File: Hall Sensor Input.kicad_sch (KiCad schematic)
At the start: 3 parts

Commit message: Getting ready for fab
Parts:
- C?: DigiKey (none) -> 490-4762-1-ND
- R? (x2): DigiKey (none) -> 311-1.00KLRCT-ND
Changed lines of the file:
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@@
     (rev "0")
     (company "Cornell High Energy Synchrotron Source")
+    (comment 1 "Hall Sensor Input Filtering")
     (comment 3 "S. Bywater")
     (comment 4 "S. Bywater")
@@
     )
     (property "Comments" "" (at 146.05 107.95 0)
+      (effects (font (size 1.27 1.27)) hide)
+    )
+    (property "DigiKey" "490-4762-1-ND" (at 146.05 107.95 0)
+      (effects (font (size 1.27 1.27)) hide)
+    )
+    (property "LCSC" "" (at 146.05 107.95 0)
       (effects (font (size 1.27 1.27)) hide)
     )
@@
       (effects (font (size 1.27 1.27)) hide)
     )
+    (property "DigiKey" "311-1.00KLRCT-ND" (at 139.7 107.95 0)
+      (effects (font (size 1.27 1.27)) hide)
+    )
+    (property "LCSC" "" (at 139.7 107.95 0)
+      (effects (font (size 1.27 1.27)) hide)
+    )
     (pin "1")
     (pin "2")
@@
       (effects (font (size 1.27 1.27)) hide)
     )
+    (property "DigiKey" "311-1.00KLRCT-ND" (at 133.35 101.6 0)
+      (effects (font (size 1.27 1.27)) hide)
+    )
+    (property "LCSC" "" (at 133.35 101.6 0)
+      (effects (font (size 1.27 1.27)) hide)
+    )

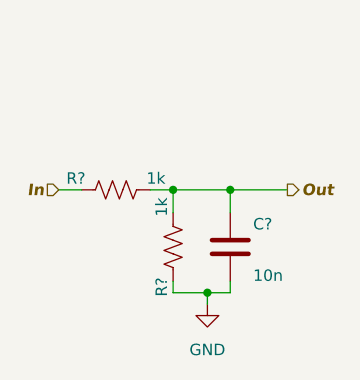
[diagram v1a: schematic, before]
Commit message: Update hall sensor circuit for 5V-tolerant pins
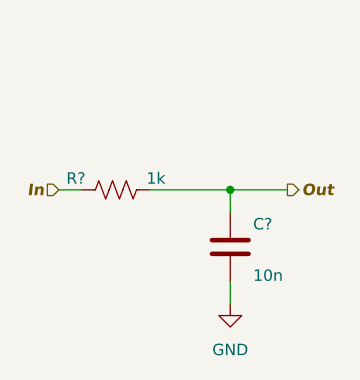
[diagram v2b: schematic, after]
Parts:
- removed R?: 1k, Resistor_SMD:R_0402_1005Metric, symbol Device:R_US
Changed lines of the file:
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@@
   (junction (at 146.05 101.6) (diameter 0) (color 0 0 0 0)
   )
-  (junction (at 139.7 101.6) (diameter 0) (color 0 0 0 0)
-  )
-  (junction (at 143.51 113.03) (diameter 0) (color 0 0 0 0)
-  )
-  (wire (pts (xy 146.05 111.76) (xy 146.05 113.03))
-    (stroke (width 0) (type default))
-  )
-  (wire (pts (xy 139.7 101.6) (xy 139.7 104.14))
+  (wire (pts (xy 146.05 111.76) (xy 146.05 114.3))
     (stroke (width 0) (type default))
   )
@@
     (stroke (width 0) (type default))
   )
-  (wire (pts (xy 143.51 113.03) (xy 146.05 113.03))
-    (stroke (width 0) (type default))
-  )
-  (wire (pts (xy 139.7 101.6) (xy 146.05 101.6))
+  (wire (pts (xy 137.16 101.6) (xy 146.05 101.6))
     (stroke (width 0) (type default))
   )
   (wire (pts (xy 146.05 101.6) (xy 152.4 101.6))
-    (stroke (width 0) (type default))
-  )
-  (wire (pts (xy 139.7 111.76) (xy 139.7 113.03))
-    (stroke (width 0) (type default))
-  )
-  (wire (pts (xy 139.7 113.03) (xy 143.51 113.03))
-    (stroke (width 0) (type default))
-  )
-  (wire (pts (xy 137.16 101.6) (xy 139.7 101.6))
-    (stroke (width 0) (type default))
-  )
-  (wire (pts (xy 143.51 113.03) (xy 143.51 114.3))
     (stroke (width 0) (type default))
   )
@@
     )
   )
-  (symbol (lib_id "power:GND") (at 143.51 114.3 0) (unit 1)
+  (symbol (lib_id "power:GND") (at 146.05 114.3 0) (unit 1)
     (in_bom yes) (on_board yes) (dnp no) (fields_autoplaced)
-    (property "Reference" "#PWR068" (at 143.51 120.65 0)
+    (property "Reference" "#PWR068" (at 146.05 120.65 0)
       (effects (font (size 1.27 1.27)) hide)
     )
-    (property "Value" "GND" (at 143.51 119.38 0)
+    (property "Value" "GND" (at 146.05 119.38 0)
       (effects (font (size 1.27 1.27)))
     )
-    (property "Footprint" "" (at 143.51 114.3 0)
+    (property "Footprint" "" (at 146.05 114.3 0)
       (effects (font (size 1.27 1.27)) hide)
     )
-    (property "Datasheet" "" (at 143.51 114.3 0)
+    (property "Datasheet" "" (at 146.05 114.3 0)
       (effects (font (size 1.27 1.27)) hide)
     )
@@
         )
       )
-    )
-  )
-  (symbol (lib_id "Device:R_US") (at 139.7 107.95 180) (unit 1)
-    (in_bom yes) (on_board yes) (dnp no)
-    (property "Reference" "R?" (at 138.43 112.395 90)
-      (effects (font (size 1.27 1.27)))
-    )
-    (property "Value" "1k" (at 138.43 103.505 90)
-      (effects (font (size 1.27 1.27)))
-    )
-    (property "Footprint" "Resistor_SMD:R_0402_1005Metric" (at 138.684 107.696 90)
-      (effects (font (size 1.27 1.27)) hide)
-    )
-    (property "Datasheet" "~" (at 139.7 107.95 0)
-      (effects (font (size 1.27 1.27)) hide)
-    )
-    (property "Comments" "" (at 139.7 107.95 0)
-      (effects (font (size 1.27 1.27)) hide)
-    )
-    (property "DigiKey" "311-1.00KLRCT-ND" (at 139.7 107.95 0)
-      (effects (font (size 1.27 1.27)) hide)
-    )
-    (property "LCSC" "" (at 139.7 107.95 0)
-      (effects (font (size 1.27 1.27)) hide)
-    )
-    (pin "1")
-    (pin "2")
-    (instances
-      (project "ECE4760 Motor Driver"
-        (path "/6b38a626-de8c-4b2d-bc76-3a02bc823a86"
-          (reference "R?") (unit 1)
-        )
-        (path "/6b38a626-de8c-4b2d-bc76-3a02bc823a86/9e0a8a8b-b0ec-4703-8f8c-5ea275317857"
-          (reference "R13") (unit 1)
-        )
-        (path "/6b38a626-de8c-4b2d-bc76-3a02bc823a86/cdc8f404-9c8e-42d0-adf1-2d432268a04d"
-          (reference "R15") (unit 1)
-        )
-        (path "/6b38a626-de8c-4b2d-bc76-3a02bc823a86/a05ea58c-77e1-4772-b7c7-450b1547e96e"
-          (reference "R17") (unit 1)
-        )
-        (path "/6b38a626-de8c-4b2d-bc76-3a02bc823a86/719c509b-8ff9-4083-837d-a3024db7e531"
-          (reference "R19") (unit 1)
-        )
-      )

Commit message: Ready for design review
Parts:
- added D?: BAT54XY, Package_TO_SOT_SMD:SOT-363_SC-70-6, symbol Diode:BAT54SW
- added R?: 4k7, Resistor_SMD:R_0402_1005Metric, symbol Device:R_US
- C?: value 10n -> 1n; DigiKey 490-4762-1-ND -> 490-GCM155R71H102KA37JCT-ND; LCSC (none) -> C1852263
- R?: value 1k -> 100; DigiKey 311-1.00KLRCT-ND -> 311-100JRCT-ND; LCSC (none) -> C106233
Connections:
- net GND: now also D?.1 (A)
- net Out: now also D?.6 (COM), R?.2
- new net +5V: D?.2 (K), R?.1

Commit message: Update
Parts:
- removed D?: BAT54XY, Package_TO_SOT_SMD:SOT-363_SC-70-6, symbol Diode:BAT54SW
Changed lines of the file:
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@@
   (junction (at 146.05 101.6) (diameter 0) (color 0 0 0 0)
   )
-  (junction (at 139.7 101.6) (diameter 0) (color 0 0 0 0)
-  )
-  (junction (at 142.875 114.935) (diameter 0) (color 0 0 0 0)
-  )
-  (junction (at 142.875 88.9) (diameter 0) (color 0 0 0 0)
-  )
-  (wire (pts (xy 139.7 93.98) (xy 139.7 88.9))
-    (stroke (width 0) (type default))
-  )
-  (wire (pts (xy 142.875 114.935) (xy 142.875 115.57))
-    (stroke (width 0) (type default))
-  )
-  (wire (pts (xy 142.875 114.935) (xy 146.05 114.935))
-    (stroke (width 0) (type default))
-  )
-  (wire (pts (xy 146.05 114.935) (xy 146.05 111.76))
-    (stroke (width 0) (type default))
-  )
-  (wire (pts (xy 139.7 114.935) (xy 142.875 114.935))
+  (wire (pts (xy 146.05 114.3) (xy 146.05 111.76))
     (stroke (width 0) (type default))
   )
@@
     (stroke (width 0) (type default))
   )
-  (wire (pts (xy 139.7 109.22) (xy 139.7 114.935))
-    (stroke (width 0) (type default))
-  )
   (wire (pts (xy 146.05 99.06) (xy 146.05 101.6))
     (stroke (width 0) (type default))
   )
-  (wire (pts (xy 142.875 88.9) (xy 146.05 88.9))
-    (stroke (width 0) (type default))
-  )
   (wire (pts (xy 127 101.6) (xy 129.54 101.6))
     (stroke (width 0) (type default))
   )
-  (wire (pts (xy 137.16 101.6) (xy 139.7 101.6))
-    (stroke (width 0) (type default))
-  )
-  (wire (pts (xy 142.875 87.63) (xy 142.875 88.9))
+  (wire (pts (xy 137.16 101.6) (xy 146.05 101.6))
     (stroke (width 0) (type default))
   )
@@
     (stroke (width 0) (type default))
   )
-  (wire (pts (xy 139.7 88.9) (xy 142.875 88.9))
-    (stroke (width 0) (type default))
-  )
   (wire (pts (xy 146.05 88.9) (xy 146.05 91.44))
-    (stroke (width 0) (type default))
-  )
-  (wire (pts (xy 139.7 101.6) (xy 146.05 101.6))
     (stroke (width 0) (type default))
   )
@@
           (reference "C63") (unit 1)
         )
-        (path "/6b38a626-de8c-4b2d-bc76-3a02bc823a86/719c509b-8ff9-4083-837d-a3024db7e531"
-          (reference "C64") (unit 1)
-        )
-      )
-    )
-  )
-  (symbol (lib_id "power:GND") (at 142.875 115.57 0) (unit 1)
+      )
+    )
+  )
+  (symbol (lib_id "power:GND") (at 146.05 114.3 0) (unit 1)
     (in_bom yes) (on_board yes) (dnp no) (fields_autoplaced)
-    (property "Reference" "#PWR02" (at 142.875 121.92 0)
-      (effects (font (size 1.27 1.27)) hide)
-    )
-    (property "Value" "GND" (at 142.875 120.65 0)
-      (effects (font (size 1.27 1.27)) hide)
-    )
-    (property "Footprint" "" (at 142.875 115.57 0)
-      (effects (font (size 1.27 1.27)) hide)
-    )
-    (property "Datasheet" "" (at 142.875 115.57 0)
+    (property "Reference" "#PWR02" (at 146.05 120.65 0)
+      (effects (font (size 1.27 1.27)) hide)
+    )
+    (property "Value" "GND" (at 146.05 119.38 0)
+      (effects (font (size 1.27 1.27)) hide)
+    )
+    (property "Footprint" "" (at 146.05 114.3 0)
+      (effects (font (size 1.27 1.27)) hide)
+    )
+    (property "Datasheet" "" (at 146.05 114.3 0)
       (effects (font (size 1.27 1.27)) hide)
     )
@@
         (path "/6b38a626-de8c-4b2d-bc76-3a02bc823a86/a05ea58c-77e1-4772-b7c7-450b1547e96e"
           (reference "#PWR06") (unit 1)
-        )
-        (path "/6b38a626-de8c-4b2d-bc76-3a02bc823a86/719c509b-8ff9-4083-837d-a3024db7e531"
-          (reference "#PWR08") (unit 1)
         )
       )
@@
           (reference "R?") (unit 1)
         )
-        (path "/6b38a626-de8c-4b2d-bc76-3a02bc823a86/3c576bdf-2a9b-47b5-bf2f-8d65e4282c90"
-          (reference "R?") (unit 1)
-        )
         (path "/6b38a626-de8c-4b2d-bc76-3a02bc823a86/9e0a8a8b-b0ec-4703-8f8c-5ea275317857"
           (reference "R12") (unit 1)
@@
           (reference "R16") (unit 1)
         )
-        (path "/6b38a626-de8c-4b2d-bc76-3a02bc823a86/719c509b-8ff9-4083-837d-a3024db7e531"
-          (reference "R18") (unit 1)
-        )
-      )
-    )
-  )
-  (symbol (lib_id "Diode:BAT54SW") (at 139.7 101.6 90) (unit 1)
-    (in_bom yes) (on_board yes) (dnp no)
-    (property "Reference" "D?" (at 137.795 93.98 90)
-      (effects (font (size 1.27 1.27)) (justify left))
-    )
-    (property "Value" "BAT54XY" (at 137.795 95.885 90)
-      (effects (font (size 1.27 1.27)) (justify left))
-    )
-    (property "Footprint" "Package_TO_SOT_SMD:SOT-363_SC-70-6" (at 143.51 101.6 0)
-      (effects (font (size 1.27 1.27)) (justify left) hide)
-    )
-    (property "Datasheet" "https://assets.nexperia.com/documents/data-sheet/BAT54W_SER.pdf" (at 143.51 101.6 0)
-      (effects (font (size 1.27 1.27)) hide)
-    )
-    (property "LCSC" "C282367" (at 139.7 101.6 0)
-      (effects (font (size 1.27 1.27)) hide)
-    )
-    (property "DigiKey" "1727-3571-1-ND" (at 139.7 101.6 0)
-      (effects (font (size 1.27 1.27)) hide)
-    )
-    (pin "1")
-    (pin "2")
-    (pin "6")
-    (pin "3")
-    (pin "4")
-    (pin "5")
-    (instances
-      (project "ECE4760 Motor Driver"
-        (path "/6b38a626-de8c-4b2d-bc76-3a02bc823a86"
-          (reference "D?") (unit 1)
-        )
-        (path "/6b38a626-de8c-4b2d-bc76-3a02bc823a86/9895140f-573d-481d-a8a6-67e4fef141c0"
-          (reference "D?") (unit 1)
-        )
-        (path "/6b38a626-de8c-4b2d-bc76-3a02bc823a86/299487ec-ee2d-43f4-ae82-35783d2e6b45"
-          (reference "D?") (unit 2)
-        )
-        (path "/6b38a626-de8c-4b2d-bc76-3a02bc823a86/5fa307ae-0220-4647-a069-86a82689cac4"
-          (reference "D?") (unit 1)
-        )
-        (path "/6b38a626-de8c-4b2d-bc76-3a02bc823a86/3c576bdf-2a9b-47b5-bf2f-8d65e4282c90"
-          (reference "D?") (unit 2)
-        )
-        (path "/6b38a626-de8c-4b2d-bc76-3a02bc823a86/9e0a8a8b-b0ec-4703-8f8c-5ea275317857"
-          (reference "D1") (unit 1)
-        )
-        (path "/6b38a626-de8c-4b2d-bc76-3a02bc823a86/cdc8f404-9c8e-42d0-adf1-2d432268a04d"
-          (reference "D1") (unit 2)
-        )
-        (path "/6b38a626-de8c-4b2d-bc76-3a02bc823a86/a05ea58c-77e1-4772-b7c7-450b1547e96e"
-          (reference "D2") (unit 1)
-        )
-        (path "/6b38a626-de8c-4b2d-bc76-3a02bc823a86/719c509b-8ff9-4083-837d-a3024db7e531"
-          (reference "D2") (unit 2)
-        )
-      )
-    )
-  )
-  (symbol (lib_id "power:+5V") (at 142.875 87.63 0) (unit 1)
+      )
+    )
+  )
+  (symbol (lib_id "power:+5V") (at 146.05 88.9 0) (unit 1)
     (in_bom yes) (on_board yes) (dnp no) (fields_autoplaced)
-    (property "Reference" "#PWR01" (at 142.875 91.44 0)
-      (effects (font (size 1.27 1.27)) hide)
-    )
-    (property "Value" "+5V" (at 142.875 83.82 0)
+    (property "Reference" "#PWR01" (at 146.05 92.71 0)
+      (effects (font (size 1.27 1.27)) hide)
+    )
+    (property "Value" "+5V" (at 146.05 85.09 0)
       (effects (font (size 1.27 1.27)))
     )
-    (property "Footprint" "" (at 142.875 87.63 0)
-      (effects (font (size 1.27 1.27)) hide)
-    )
-    (property "Datasheet" "" (at 142.875 87.63 0)
+    (property "Footprint" "" (at 146.05 88.9 0)
+      (effects (font (size 1.27 1.27)) hide)
+    )
+    (property "Datasheet" "" (at 146.05 88.9 0)
       (effects (font (size 1.27 1.27)) hide)
     )
@@
         (path "/6b38a626-de8c-4b2d-bc76-3a02bc823a86/a05ea58c-77e1-4772-b7c7-450b1547e96e"
           (reference "#PWR05") (unit 1)
-        )
-        (path "/6b38a626-de8c-4b2d-bc76-3a02bc823a86/719c509b-8ff9-4083-837d-a3024db7e531"
-          (reference "#PWR07") (unit 1)
         )
       )
@@
           (reference "R17") (unit 1)
         )
-        (path "/6b38a626-de8c-4b2d-bc76-3a02bc823a86/719c509b-8ff9-4083-837d-a3024db7e531"
-          (reference "R19") (unit 1)
-        )
-      )
+      )

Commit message: Boards ordered!
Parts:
- C?: LCSC C1852263 -> C277522
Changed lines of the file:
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@@
       (effects (font (size 1.27 1.27)) hide)
     )
-    (property "LCSC" "C1852263" (at 146.05 107.95 0)
+    (property "LCSC" "C277522" (at 146.05 107.95 0)
       (effects (font (size 1.27 1.27)) hide)
     )
@@
         )
         (path "/6b38a626-de8c-4b2d-bc76-3a02bc823a86/9e0a8a8b-b0ec-4703-8f8c-5ea275317857"
-          (reference "C61") (unit 1)
+          (reference "C43") (unit 1)
         )
         (path "/6b38a626-de8c-4b2d-bc76-3a02bc823a86/cdc8f404-9c8e-42d0-adf1-2d432268a04d"
-          (reference "C62") (unit 1)
+          (reference "C44") (unit 1)
         )
         (path "/6b38a626-de8c-4b2d-bc76-3a02bc823a86/a05ea58c-77e1-4772-b7c7-450b1547e96e"
-          (reference "C63") (unit 1)
+          (reference "C45") (unit 1)
         )
       )
@@
   (symbol (lib_id "power:GND") (at 146.05 114.3 0) (unit 1)
     (in_bom yes) (on_board yes) (dnp no) (fields_autoplaced)
-    (property "Reference" "#PWR02" (at 146.05 120.65 0)
+    (property "Reference" "#PWR072" (at 146.05 120.65 0)
       (effects (font (size 1.27 1.27)) hide)
     )
@@
       (project "ECE4760 Motor Driver"
         (path "/6b38a626-de8c-4b2d-bc76-3a02bc823a86/9e0a8a8b-b0ec-4703-8f8c-5ea275317857"
-          (reference "#PWR02") (unit 1)
+          (reference "#PWR072") (unit 1)
         )
         (path "/6b38a626-de8c-4b2d-bc76-3a02bc823a86/cdc8f404-9c8e-42d0-adf1-2d432268a04d"
-          (reference "#PWR04") (unit 1)
+          (reference "#PWR074") (unit 1)
         )
         (path "/6b38a626-de8c-4b2d-bc76-3a02bc823a86/a05ea58c-77e1-4772-b7c7-450b1547e96e"
-          (reference "#PWR06") (unit 1)
+          (reference "#PWR076") (unit 1)
         )
       )
@@
         )
         (path "/6b38a626-de8c-4b2d-bc76-3a02bc823a86/9e0a8a8b-b0ec-4703-8f8c-5ea275317857"
-          (reference "R12") (unit 1)
+          (reference "R13") (unit 1)
         )
         (path "/6b38a626-de8c-4b2d-bc76-3a02bc823a86/cdc8f404-9c8e-42d0-adf1-2d432268a04d"
-          (reference "R14") (unit 1)
+          (reference "R15") (unit 1)
         )
         (path "/6b38a626-de8c-4b2d-bc76-3a02bc823a86/a05ea58c-77e1-4772-b7c7-450b1547e96e"
-          (reference "R16") (unit 1)
+          (reference "R17") (unit 1)
         )
       )
@@
   (symbol (lib_id "power:+5V") (at 146.05 88.9 0) (unit 1)
     (in_bom yes) (on_board yes) (dnp no) (fields_autoplaced)
-    (property "Reference" "#PWR01" (at 146.05 92.71 0)
+    (property "Reference" "#PWR071" (at 146.05 92.71 0)
       (effects (font (size 1.27 1.27)) hide)
     )
@@
       (project "ECE4760 Motor Driver"
         (path "/6b38a626-de8c-4b2d-bc76-3a02bc823a86/9e0a8a8b-b0ec-4703-8f8c-5ea275317857"
-          (reference "#PWR01") (unit 1)
+          (reference "#PWR071") (unit 1)
         )
         (path "/6b38a626-de8c-4b2d-bc76-3a02bc823a86/cdc8f404-9c8e-42d0-adf1-2d432268a04d"
-          (reference "#PWR03") (unit 1)
+          (reference "#PWR073") (unit 1)
         )
         (path "/6b38a626-de8c-4b2d-bc76-3a02bc823a86/a05ea58c-77e1-4772-b7c7-450b1547e96e"
-          (reference "#PWR05") (unit 1)
+          (reference "#PWR075") (unit 1)
         )
       )
@@
         )
         (path "/6b38a626-de8c-4b2d-bc76-3a02bc823a86/9e0a8a8b-b0ec-4703-8f8c-5ea275317857"
-          (reference "R13") (unit 1)
+          (reference "R14") (unit 1)
         )
         (path "/6b38a626-de8c-4b2d-bc76-3a02bc823a86/cdc8f404-9c8e-42d0-adf1-2d432268a04d"
-          (reference "R15") (unit 1)
+          (reference "R16") (unit 1)
         )
         (path "/6b38a626-de8c-4b2d-bc76-3a02bc823a86/a05ea58c-77e1-4772-b7c7-450b1547e96e"
-          (reference "R17") (unit 1)
+          (reference "R18") (unit 1)
         )
       )
